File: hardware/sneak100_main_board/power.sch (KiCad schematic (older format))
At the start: 21 parts, among them J10 Conn_01x02, J9 Conn_01x03, Q1 Q_PMOS_DGS, Q2 Q_PMOS_DGS, SW3 SW_Push_SPDT, U6 LM1117-3.3

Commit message: USB FDU mode
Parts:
- added C9: 780uF, Capacitor_THT:CP_Radial_D10.0mm_P5.00mm, symbol Device:CP
- C11: renamed from C13; footprint Capacitor_SMD:CP_Elec_4x3 -> Capacitor_Tantalum_SMD:CP_EIA-1608-10_AVX-L
- C12: renamed from C14; footprint Capacitor_SMD:CP_Elec_4x3 -> Capacitor_Tantalum_SMD:CP_EIA-1608-10_AVX-L
- renumbered C12 to C10, C15 to C13, D4 to D1, D5 to D2, D6 to D3, J9 to J5, J10 to J6, R10 to R1, R11 to R2, R12 to R3, R13 to R4, R14 to R5, R15 to R6, R16 to R7, R17 to R8, SW3 to SW1, U6 to U5
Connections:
- net GND: now also C9.2
- net at J6.1 (Pin_1), Q1.1 (D): now also C9.1

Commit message: delete USB, modify top hull, bigger PCB board
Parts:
- SW1: footprint Button_Switch_SMD:SW_SPDT_CK-JS102011SAQN -> Connector_PinHeader_2.54mm:PinHeader_1x03_P2.54mm_Vertical
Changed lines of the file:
@@
 F 0 "SW1" H 4050 3100 50  0000 C CNN
 F 1 "SW_Push_SPDT" H 4050 3000 50  0000 C CNN
-F 2 "Button_Switch_SMD:SW_SPDT_CK-JS102011SAQN" H 3500 3050 50  0001 C CNN
+F 2 "Connector_PinHeader_2.54mm:PinHeader_1x03_P2.54mm_Vertical" H 3500 3050 50  0001 C CNN
 F 3 "~" H 3500 3050 50  0001 C CNN
 	1    3500 3050

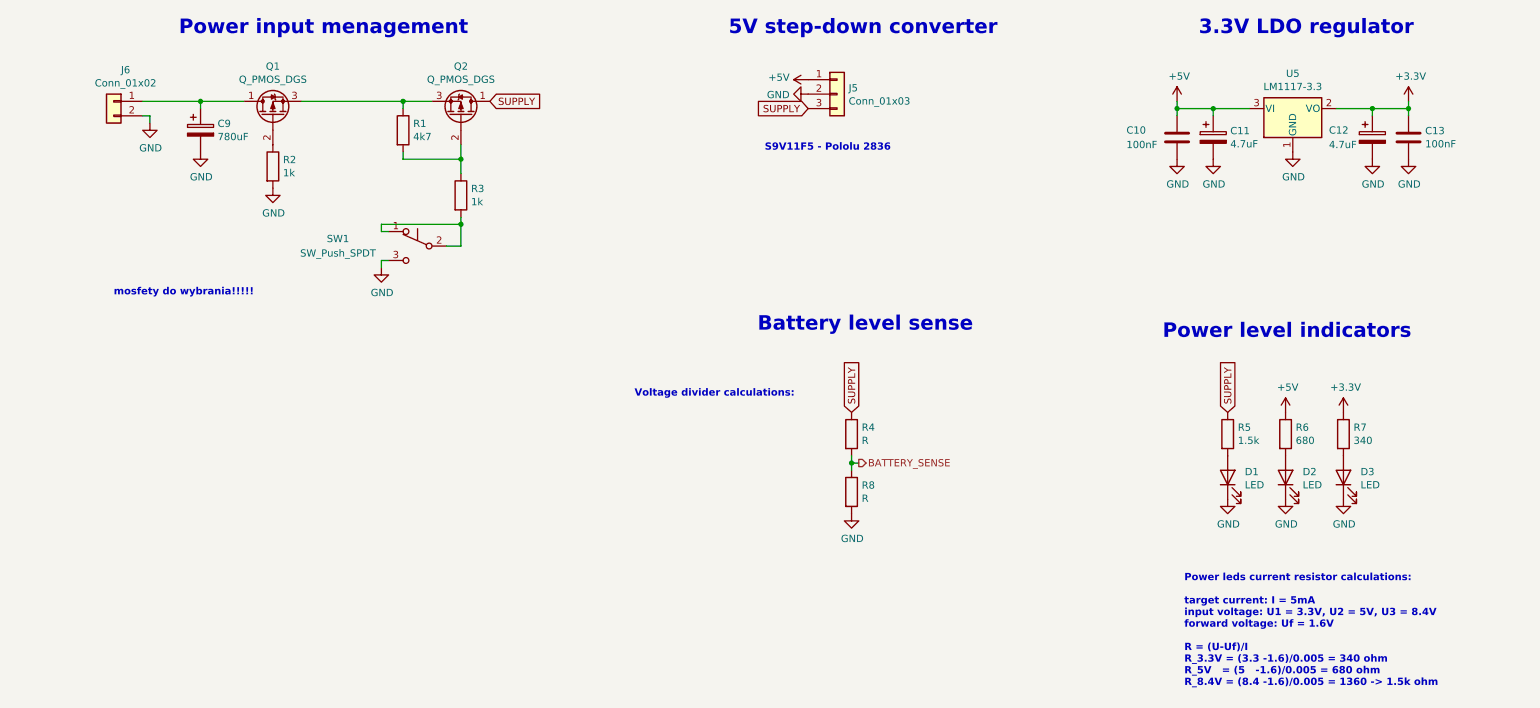
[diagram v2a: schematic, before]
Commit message: Board interface layout
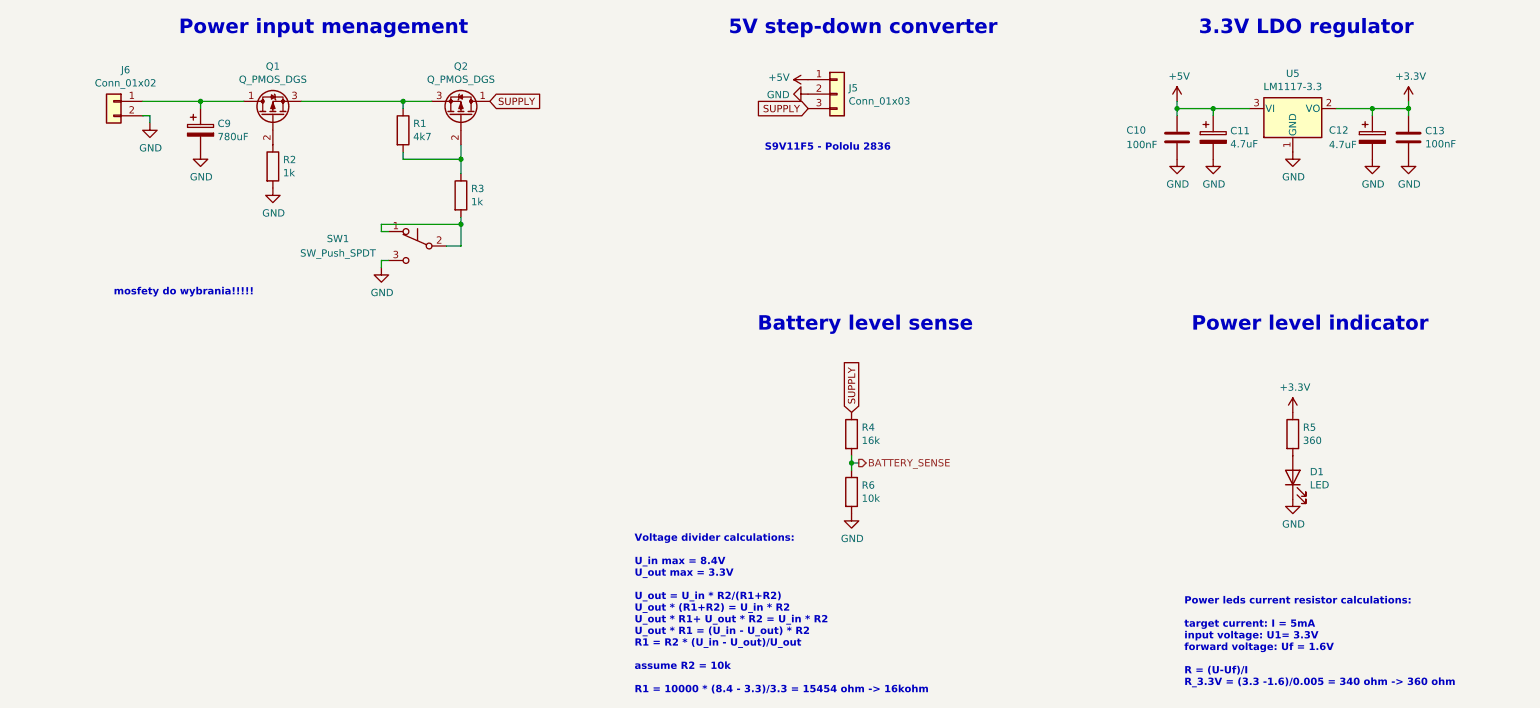
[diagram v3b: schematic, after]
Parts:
- removed D1, D2: LED, LED_SMD:LED_0603_1608Metric, symbol Device:LED
- removed R5: 1.5k, Resistor_SMD:R_0603_1608Metric, symbol Device:R
- removed R6: 680, Resistor_SMD:R_0603_1608Metric, symbol Device:R
- R4: value R -> 16k
- R5: renamed from R7; value 340 -> 360
- R6: renamed from R8; value R -> 10k
- renumbered D3 to D1
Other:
- note added: "Power leds current resistor calculations:\n\ntarget current: I = 5mA\ninput voltage: U1= 3.3V\nforward voltage: Uf = 1.6V\n\nR = (U-Uf)/I\nR_3.3V = (3.3 -1.6)/0.005 = 340 ohm -> 360 ohm"
- note added: "Power level indicator"
- note added: "Voltage divider calculations:\n\nU_in max = 8.4V\nU_out max = 3.3V\n\nU_out = U_in * R2/(R1+R2)\nU_out * (R1+R2) = U_in * R2\nU_out * R1+ U_out * R2 = U_in * R2\nU_out * R1 = (U_in - U_out) * R2\nR1 = R2 * (U_in - U_out)/U_out\n\nassume R2 = 10k\n\nR1 = 10000 * (8.4 - 3.3)/3.3 = 15454 ohm -> 16kohm\n"
- note removed: "Power leds current resistor calculations:\n\ntarget current: I = 5mA\ninput voltage: U1 = 3.3V, U2 = 5V, U3 = 8.4V\nforward voltage: Uf = 1.6V\n\nR = (U-Uf)/I\nR_3.3V = (3.3 -1.6)/0.005 = 340 ohm\nR_5V = (5 -1.6)/0.005 = 680 ohm\nR_8.4V = (8.4 -1.6)/0.005 = 1360 -> 1.5k ohm"
- note removed: "Power level indicators"
- note removed: "Voltage divider calculations:"
- moved on the sheet: D1, R5
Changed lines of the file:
@@
 SUPPLY
 $Comp
-L Device:LED D2
-U 1 1 60F0446D
-P 9500 4650
-F 0 "D2" V 9539 4532 50  0000 R CNN
-F 1 "LED" V 9448 4532 50  0000 R CNN
-F 2 "LED_SMD:LED_0603_1608Metric" H 9500 4650 50  0001 C CNN
-F 3 "~" H 9500 4650 50  0001 C CNN
-	1    9500 4650
+L Device:LED D1
+U 1 1 60F07A86
+P 9550 4650
+F 0 "D1" V 9589 4532 50  0000 R CNN
+F 1 "LED" V 9498 4532 50  0000 R CNN
+F 2 "LED_SMD:LED_0603_1608Metric" H 9550 4650 50  0001 C CNN
+F 3 "~" H 9550 4650 50  0001 C CNN
+	1    9550 4650
 	0    -1   -1   0
 $EndComp
 $Comp
-L Device:R R6
-U 1 1 60F051F0
-P 9500 4350
-F 0 "R6" H 9570 4396 50  0000 L CNN
-F 1 "680" H 9570 4305 50  0000 L CNN
-F 2 "Resistor_SMD:R_0603_1608Metric" V 9430 4350 50  0001 C CNN
-F 3 "~" H 9500 4350 50  0001 C CNN
-	1    9500 4350
-	1    0    0    -1
-$EndComp
-$Comp
-L power:GND #PWR049
-U 1 1 60F05D55
-P 9500 4800
-F 0 "#PWR049" H 9500 4550 50  0001 C CNN
-F 1 "GND" H 9505 4627 50  0000 C CNN
-F 2 "" H 9500 4800 50  0001 C CNN
-F 3 "" H 9500 4800 50  0001 C CNN
-	1    9500 4800
-	1    0    0    -1
-$EndComp
-$Comp
-L power:+5V #PWR046
-U 1 1 60F06197
-P 9500 4200
-F 0 "#PWR046" H 9500 4050 50  0001 C CNN
-F 1 "+5V" H 9515 4373 50  0000 C CNN
-F 2 "" H 9500 4200 50  0001 C CNN
-F 3 "" H 9500 4200 50  0001 C CNN
-	1    9500 4200
-	1    0    0    -1
-$EndComp
-$Comp
-L Device:LED D3
-U 1 1 60F07A86
-P 9900 4650
-F 0 "D3" V 9939 4532 50  0000 R CNN
-F 1 "LED" V 9848 4532 50  0000 R CNN
-F 2 "LED_SMD:LED_0603_1608Metric" H 9900 4650 50  0001 C CNN
-F 3 "~" H 9900 4650 50  0001 C CNN
-	1    9900 4650
-	0    -1   -1   0
-$EndComp
-$Comp
-L Device:R R7
+L Device:R R5
 U 1 1 60F07A8C
-P 9900 4350
-F 0 "R7" H 9970 4396 50  0000 L CNN
-F 1 "340" H 9970 4305 50  0000 L CNN
-F 2 "Resistor_SMD:R_0603_1608Metric" V 9830 4350 50  0001 C CNN
-F 3 "~" H 9900 4350 50  0001 C CNN
-	1    9900 4350
-	1    0    0    -1
-$EndComp
-$Comp
-L power:GND #PWR050
+P 9550 4350
+F 0 "R5" H 9620 4396 50  0000 L CNN
+F 1 "360" H 9620 4305 50  0000 L CNN
+F 2 "Resistor_SMD:R_0603_1608Metric" V 9480 4350 50  0001 C CNN
+F 3 "~" H 9550 4350 50  0001 C CNN
+	1    9550 4350
+	1    0    0    -1
+$EndComp
+$Comp
+L power:GND #PWR047
 U 1 1 60F07A92
-P 9900 4800
-F 0 "#PWR050" H 9900 4550 50  0001 C CNN
-F 1 "GND" H 9905 4627 50  0000 C CNN
-F 2 "" H 9900 4800 50  0001 C CNN
-F 3 "" H 9900 4800 50  0001 C CNN
-	1    9900 4800
-	1    0    0    -1
-$EndComp
-$Comp
-L power:+3.3V #PWR047
+P 9550 4800
+F 0 "#PWR047" H 9550 4550 50  0001 C CNN
+F 1 "GND" H 9555 4627 50  0000 C CNN
+F 2 "" H 9550 4800 50  0001 C CNN
+F 3 "" H 9550 4800 50  0001 C CNN
+	1    9550 4800
+	1    0    0    -1
+$EndComp
+$Comp
+L power:+3.3V #PWR046
 U 1 1 60F07C02
-P 9900 4200
-F 0 "#PWR047" H 9900 4050 50  0001 C CNN
-F 1 "+3.3V" H 9915 4373 50  0000 C CNN
-F 2 "" H 9900 4200 50  0001 C CNN
-F 3 "" H 9900 4200 50  0001 C CNN
-	1    9900 4200
-	1    0    0    -1
-$EndComp
-$Comp
-L Device:LED D1
-U 1 1 60F0A82A
-P 9100 4650
-F 0 "D1" V 9139 4532 50  0000 R CNN
-F 1 "LED" V 9048 4532 50  0000 R CNN
-F 2 "LED_SMD:LED_0603_1608Metric" H 9100 4650 50  0001 C CNN
-F 3 "~" H 9100 4650 50  0001 C CNN
-	1    9100 4650
-	0    -1   -1   0
-$EndComp
-$Comp
-L Device:R R5
-U 1 1 60F0A830
-P 9100 4350
-F 0 "R5" H 9170 4396 50  0000 L CNN
-F 1 "1.5k" H 9170 4305 50  0000 L CNN
-F 2 "Resistor_SMD:R_0603_1608Metric" V 9030 4350 50  0001 C CNN
-F 3 "~" H 9100 4350 50  0001 C CNN
-	1    9100 4350
-	1    0    0    -1
-$EndComp
-$Comp
-L power:GND #PWR048
-U 1 1 60F0A836
-P 9100 4800
-F 0 "#PWR048" H 9100 4550 50  0001 C CNN
-F 1 "GND" H 9105 4627 50  0000 C CNN
-F 2 "" H 9100 4800 50  0001 C CNN
-F 3 "" H 9100 4800 50  0001 C CNN
-	1    9100 4800
-	1    0    0    -1
-$EndComp
-Text GLabel 9100 4200 1    50   Input ~ 0
-SUPPLY
+P 9550 4200
+F 0 "#PWR046" H 9550 4050 50  0001 C CNN
+F 1 "+3.3V" H 9565 4373 50  0000 C CNN
+F 2 "" H 9550 4200 50  0001 C CNN
+F 3 "" H 9550 4200 50  0001 C CNN
+	1    9550 4200
+	1    0    0    -1
+$EndComp
 Text Notes 5650 1600 0    100  ~ 20
 5V step-down converter
@@
 P 6500 4350
 F 0 "R4" H 6570 4396 50  0000 L CNN
-F 1 "R" H 6570 4305 50  0000 L CNN
+F 1 "16k" H 6570 4305 50  0000 L CNN
 F 2 "Resistor_SMD:R_0603_1608Metric" V 6430 4350 50  0001 C CNN
 F 3 "~" H 6500 4350 50  0001 C CNN
@@
 $EndComp
 $Comp
-L Device:R R8
+L Device:R R6
 U 1 1 60F10A9C
 P 6500 4750
-F 0 "R8" H 6570 4796 50  0000 L CNN
-F 1 "R" H 6570 4705 50  0000 L CNN
+F 0 "R6" H 6570 4796 50  0000 L CNN
+F 1 "10k" H 6570 4705 50  0000 L CNN
 F 2 "Resistor_SMD:R_0603_1608Metric" V 6430 4750 50  0001 C CNN
 F 3 "~" H 6500 4750 50  0001 C CNN
@@
 $EndComp
 $Comp
-L power:GND #PWR051
+L power:GND #PWR048
 U 1 1 60F10E65
 P 6500 4900
-F 0 "#PWR051" H 6500 4650 50  0001 C CNN
+F 0 "#PWR048" H 6500 4650 50  0001 C CNN
 F 1 "GND" H 6505 4727 50  0000 C CNN
 F 2 "" H 6500 4900 50  0001 C CNN
@@
 Text Notes 5850 3650 0    100  ~ 20
 Battery level sense
-Text Notes 8650 3700 0    100  ~ 20
-Power level indicators
+Text Notes 8850 3650 0    100  ~ 20
+Power level indicator
 $Comp
 L Device:R R2
@@
 Text Notes 1400 3400 0    50   ~ 10
 mosfety do wybrania!!!!!
-Text Notes 5000 4100 0    50   ~ 10
-Voltage divider calculations:
+Text Notes 5000 6150 0    50   ~ 10
+Voltage divider calculations:\n\nU_in max = 8.4V\nU_out max = 3.3V\n\nU_out = U_in * R2/(R1+R2)\nU_out * (R1+R2) = U_in * R2\nU_out * R1+ U_out * R2 = U_in * R2\nU_out * R1 = (U_in - U_out) * R2\nR1 = R2 * (U_in - U_out)/U_out\n\nassume R2 = 10k\n\nR1 = 10000 * (8.4 - 3.3)/3.3 = 15454 ohm -> 16kohm\n
 Text Notes 8800 6100 0    50   ~ 10
-Power leds current resistor calculations:\n\ntarget current: I = 5mA\ninput voltage: U1 = 3.3V, U2 = 5V, U3 = 8.4V\nforward voltage: Uf = 1.6V\n\nR = (U-Uf)/I\nR_3.3V = (3.3 -1.6)/0.005 = 340 ohm\nR_5V   = (5   -1.6)/0.005 = 680 ohm\nR_8.4V = (8.4 -1.6)/0.005 = 1360 -> 1.5k ohm
+Power leds current resistor calculations:\n\ntarget current: I = 5mA\ninput voltage: U1= 3.3V\nforward voltage: Uf = 1.6V\n\nR = (U-Uf)/I\nR_3.3V = (3.3 -1.6)/0.005 = 340 ohm -> 360 ohm
 Text Notes 5900 2400 0    50   ~ 10
 S9V11F5 - Pololu 2836

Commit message: PCB first full layout
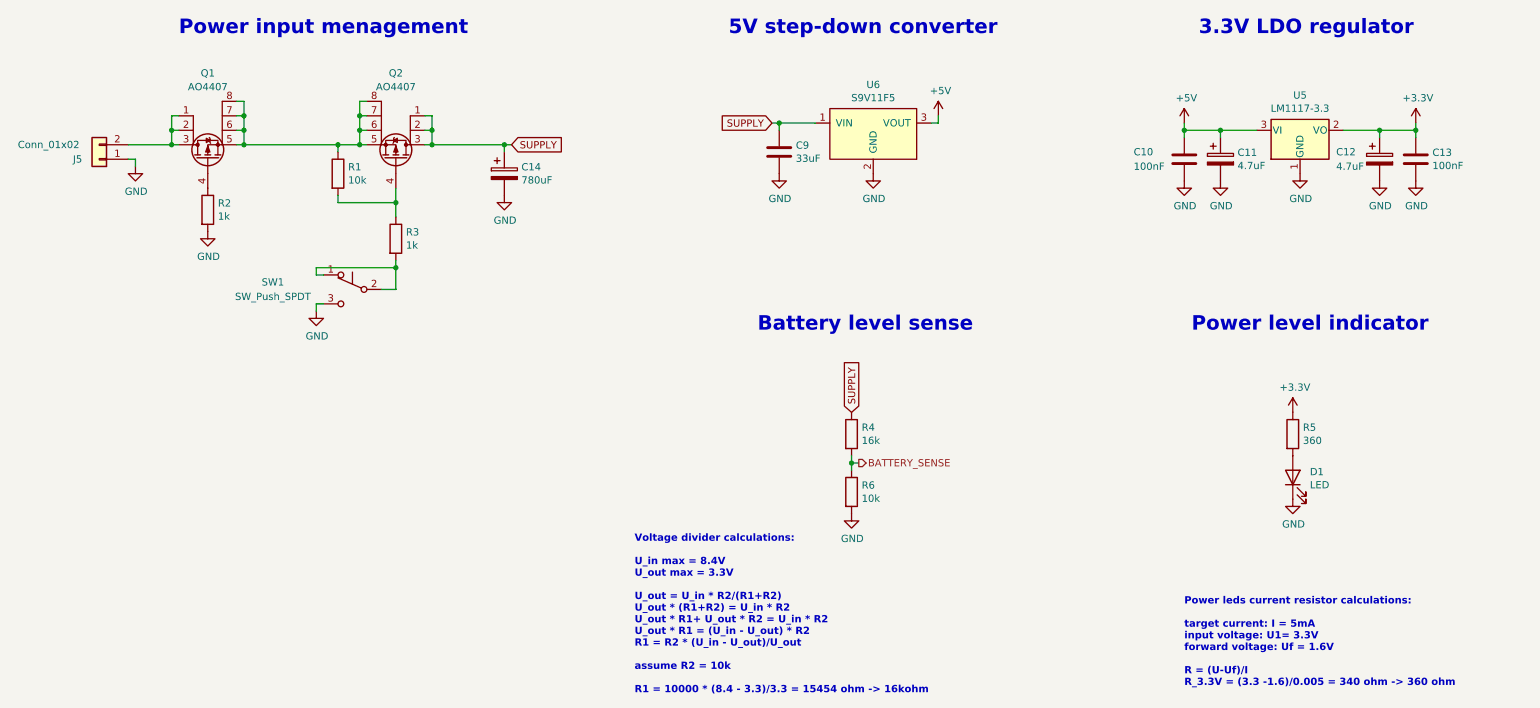
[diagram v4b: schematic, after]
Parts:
- removed J5: Conn_01x03, Connector_PinHeader_2.54mm:PinHeader_1x03_P2.54mm_Vertical, symbol Connector_Generic:Conn_01x03
- removed Q1, Q2: Q_PMOS_DGS, Package_TO_SOT_SMD:SOT-23, symbol Device:Q_PMOS_DGS
- added C9: 33uF, Capacitor_SMD:C_0805_2012Metric, symbol Device:C
- added Q1, Q2: AO4407, Package_SO:SOIC-8_3.9x4.9mm_P1.27mm, symbol Sneak100_kicad:AO4407
- added U6: S9V11F5, sneak100_lib:S9V11F5_module, symbol Sneak100_kicad:S9V11F5
- C11, C12: footprint Capacitor_Tantalum_SMD:CP_EIA-1608-10_AVX-L -> Capacitor_Tantalum_SMD:CP_EIA-3216-18_Kemet-A
- J5: renamed from J6; footprint Connector_PinHeader_2.54mm:PinHeader_1x02_P2.54mm_Vertical -> Connector_PinHeader_2.54mm:PinHeader_1x02_P2.54mm_Horizontal
- R1: value 4k7 -> 10k
- SW1: footprint Connector_PinHeader_2.54mm:PinHeader_1x03_P2.54mm_Vertical -> sneak100_lib:ESP2010_90
- renumbered C9 to C14
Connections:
- net +5V: now also U6.3 (VOUT)
- net GND: now also J5.1 (Pin_1), C9.2, U6.2 (GND); no longer J5.2 (Pin_2)
- net SUPPLY: now also C14.1, C9.1, Q2.1, Q2.2, Q2.3, U6.1 (VIN)
- net at R2.1: now also Q1.4
- net at R1.1: now also Q1.5, Q1.6, Q1.7, Q1.8, Q2.5, Q2.6, Q2.7, Q2.8
- net at R1.2, R3.1: now also Q2.4
- new net: J5.2 (Pin_2), Q1.1, Q1.2, Q1.3
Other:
- note removed: "S9V11F5 - Pololu 2836"
- note removed: "mosfety do wybrania!!!!!"
- moved on the sheet: C10, C11, C12, C13, C14, J5, R1, R2, R3, SW1, U5
